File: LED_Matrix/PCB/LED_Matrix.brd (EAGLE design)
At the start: 32 x 32 mm, 8 parts, among them U1 ATTINY48, U2 ULN2803AFWG

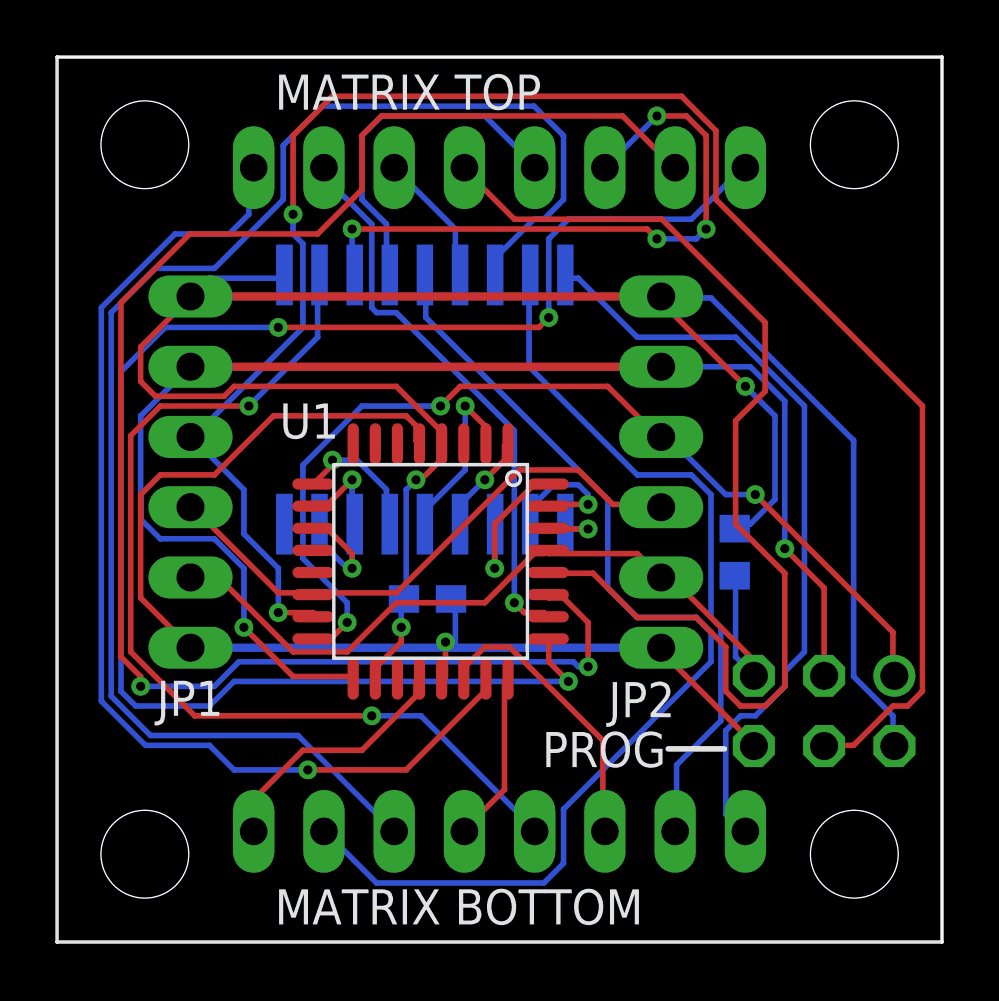
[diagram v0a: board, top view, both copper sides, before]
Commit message: led matrix - Moved library parts local.  Added rev and copyright.
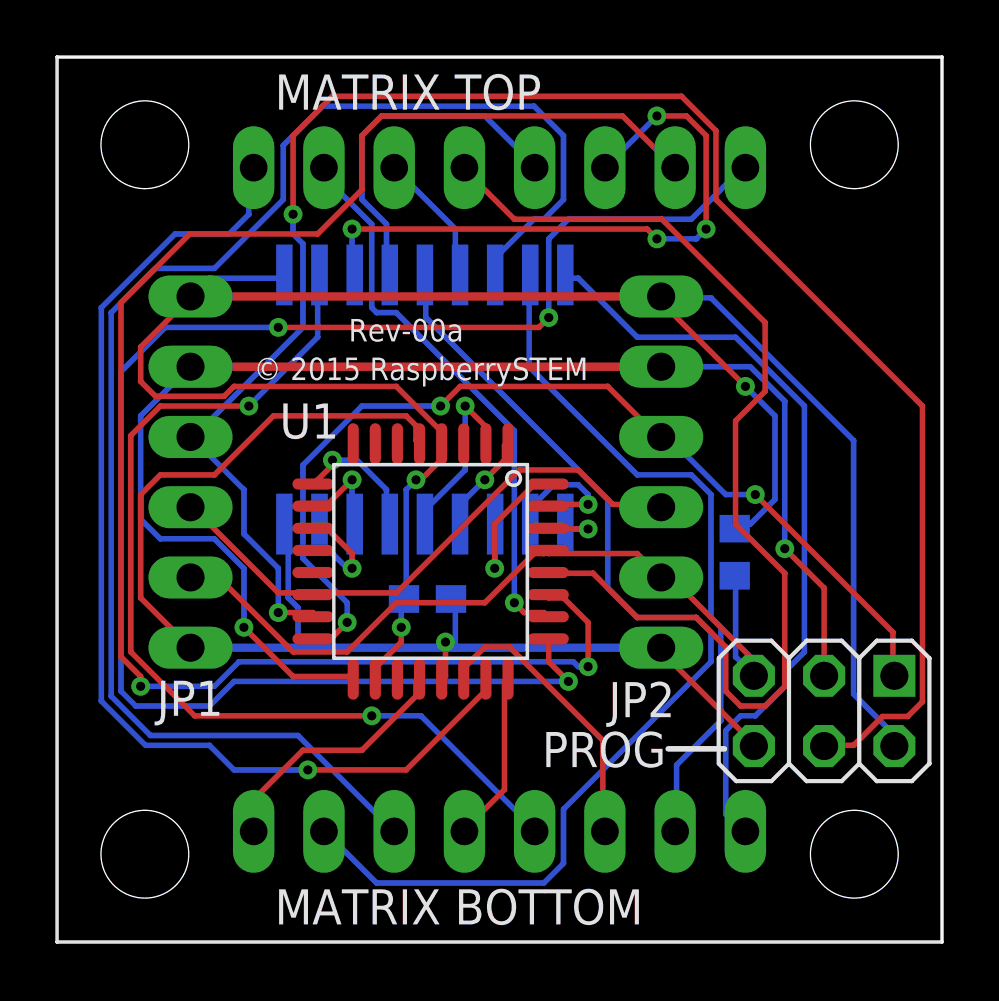
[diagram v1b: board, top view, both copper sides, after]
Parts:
- JP1, JP2: device raspberrystem:1X06 -> LED_Matrix:1X06
- LEDMATRIX: device raspberrystem:8X8_LED_MATRIX -> LED_Matrix:8X8_LED_MATRIX
- PROG: device raspberrystem:MA03-2 -> LED_Matrix:2X03
- U1: device raspberrystem:ATTINY48 -> LED_Matrix:ATTINY48
- U2: device raspberrystem:ULN2803AFWG -> LED_Matrix:ULN2803AFWG
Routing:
- net GND: track 43.7 -> 48.4 mm
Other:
- board text added: "Rev-00a"
- board text added: "© 2015 RaspberrySTEM"
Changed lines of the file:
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@@
 <layer number="56" name="wert" color="7" fill="1" visible="no" active="no"/>
 <layer number="57" name="tCAD" color="7" fill="1" visible="no" active="no"/>
+<layer number="90" name="Modules" color="5" fill="1" visible="no" active="no"/>
 <layer number="91" name="Nets" color="2" fill="1" visible="no" active="no"/>
 <layer number="92" name="Busses" color="1" fill="1" visible="no" active="no"/>
@@
 <wire x1="27.94" y1="13.208" x2="0.381" y2="13.208" width="0.2032" layer="22"/>
 <wire x1="28.829" y1="15.748" x2="0.381" y2="15.748" width="0.2032" layer="22"/>
-<wire x1="26.797" y1="18.288" x2="2.286" y2="18.288" width="0.2032" layer="22"/>
+<wire x1="27.686" y1="18.288" x2="2.286" y2="18.288" width="0.2032" layer="22"/>
 <wire x1="27.686" y1="20.828" x2="0.381" y2="20.828" width="0.2032" layer="22"/>
 <wire x1="27.686" y1="23.368" x2="0.381" y2="23.368" width="0.2032" layer="22"/>
@@
 <text x="2.032" y="17.78" size="1.27" layer="22" font="vector" rot="MR0">IN</text>
 <rectangle x1="0" y1="17.399" x2="2.413" y2="19.431" layer="43"/>
+<text x="7.112" y="20.32" size="0.8128" layer="21">© 2015 RaspberrySTEM</text>
+<text x="10.541" y="21.717" size="0.8128" layer="21">Rev-00a</text>
 </plain>
 <attributes>
@@
 <description language="de">&lt;b&gt;EAGLE Design Rules&lt;/b&gt;
 &lt;p&gt;
-Die Standard-Design-Rules sind so gewÃ¤hlt, dass sie fÃ¼r
+Die Standard-Design-Rules sind so gewÃÂ¤hlt, dass sie fÃÂ¼r
 die meisten Anwendungen passen. Sollte ihre Platine
 besondere Anforderungen haben, treffen Sie die erforderlichen
@@
 </autorouter>
 <elements>
-<element name="U1" library="raspberrystem" package="ATTINY48" value="ATTINY48" x="13.508" y="13.761" smashed="yes" rot="R270">
+<element name="U1" library="LED_Matrix" package="ATTINY48" value="ATTINY48" x="13.508" y="13.761" smashed="yes" rot="R270">
 <attribute name="NAME" x="8.047" y="18.206" size="1.27" layer="21"/>
 </element>
-<element name="U2" library="raspberrystem" package="ULN2803AFWG" value="ULN2803AFWG" x="18.381" y="15.111" smashed="yes" rot="MR0">
+<element name="U2" library="LED_Matrix" package="ULN2803AFWG" value="ULN2803AFWG" x="18.381" y="15.111" smashed="yes" rot="MR0">
 <attribute name="NAME" x="7.205" y="24.636" size="1.27" layer="22" rot="MR0"/>
 </element>
-<element name="LEDMATRIX" library="raspberrystem" package="8X8_LED_MATRIX" value="8X8_LED_MATRIX" x="16" y="16"/>
+<element name="LEDMATRIX" library="LED_Matrix" package="8X8_LED_MATRIX" value="8X8_LED_MATRIX" x="16" y="16"/>
 <element name="R1" library="resistor" package="R0603" value="10k" x="24.5048" y="14.096" smashed="yes" rot="MR270">
 <attribute name="NAME" x="23.3618" y="12.445" size="1.016" layer="26" rot="MR180"/>
@@
 <attribute name="NAME" x="14.5382" y="11.8946" size="1.016" layer="26" rot="MR180"/>
 </element>
-<element name="PROG" library="raspberrystem" package="MA03-2" value="NONE" x="27.7368" y="8.3566" smashed="yes" rot="R180">
-<attribute name="OC_NEWARK" value="unknown" x="27.7368" y="8.3566" size="1.778" layer="27" rot="R180" display="off"/>
-<attribute name="MPN" value="" x="27.7368" y="8.3566" size="1.778" layer="27" rot="R180" display="off"/>
-<attribute name="MF" value="" x="27.7368" y="8.3566" size="1.778" layer="27" rot="R180" display="off"/>
-<attribute name="OC_FARNELL" value="unknown" x="27.7368" y="8.3566" size="1.778" layer="27" rot="R180" display="off"/>
+<element name="PROG" library="LED_Matrix" package="2X03" value="NONE" x="27.7368" y="8.3566" smashed="yes" rot="R180">
 <attribute name="NAME" x="22.0218" y="7.5946" size="1.27" layer="25" ratio="10" rot="R180"/>
 </element>
-<element name="JP1" library="raspberrystem" package="1X06" value="NONE" x="4.826" y="16.9926" smashed="yes" rot="R270">
+<element name="JP1" library="LED_Matrix" package="1X06" value="NONE" x="4.826" y="16.9926" smashed="yes" rot="R270">
 <attribute name="NAME" x="3.6068" y="8.1788" size="1.27" layer="25" ratio="10"/>
 </element>
-<element name="JP2" library="raspberrystem" package="1X06" value="NONE" x="21.844" y="16.9926" smashed="yes" rot="R270">
+<element name="JP2" library="LED_Matrix" package="1X06" value="NONE" x="21.844" y="16.9926" smashed="yes" rot="R270">
 <attribute name="NAME" x="19.939" y="8.128" size="1.27" layer="25" ratio="10"/>
 </element>
@@
 <wire x1="12.6238" y1="12.446" x2="12.5452" y2="12.4026" width="0.2032" layer="16"/>
 <wire x1="13.8684" y1="17.9578" x2="13.908" y2="18.011" width="0.2032" layer="1"/>
-<wire x1="30.226" y1="8.1788" x2="30.226" y2="7.112" width="0.2032" layer="16"/>
-<wire x1="28.8036" y1="9.6012" x2="30.226" y2="8.1788" width="0.2032" layer="16"/>
-<wire x1="28.8036" y1="18.1356" x2="28.8036" y2="9.6012" width="0.2032" layer="16"/>
+<wire x1="30.226" y1="7.5438" x2="30.226" y2="7.112" width="0.2032" layer="16"/>
+<wire x1="28.8036" y1="8.9662" x2="30.226" y2="7.5438" width="0.2032" layer="16"/>
+<wire x1="28.8036" y1="18.1356" x2="28.8036" y2="8.9662" width="0.2032" layer="16"/>
 <wire x1="23.6474" y1="23.2918" x2="28.8036" y2="18.1356" width="0.2032" layer="16"/>
 <wire x1="21.8694" y1="23.2918" x2="23.6474" y2="23.2918" width="0.2032" layer="16"/>
@@
 <contactref element="JP1" pad="6"/>
 <contactref element="JP2" pad="6"/>
-<wire x1="4.826" y1="10.6426" x2="14.0462" y2="10.6426" width="0.3048" layer="16"/>
+<wire x1="4.826" y1="10.6426" x2="8.7122" y2="10.6426" width="0.3048" layer="16"/>
+<wire x1="8.7122" y1="10.6426" x2="14.0462" y2="10.6426" width="0.3048" layer="16"/>
 <wire x1="14.0462" y1="10.6426" x2="14.4018" y2="10.6426" width="0.3048" layer="16"/>
 <wire x1="14.4018" y1="10.6426" x2="21.844" y2="10.6426" width="0.3048" layer="16"/>
@@
 <via x="14.0462" y="10.8458" extent="1-16" drill="0.3302"/>
 <contactref element="U2" pad="GND"/>
-<wire x1="5.6896" y1="16.891" x2="8.221" y2="15.111" width="0" layer="19" extent="1-16"/>
+<wire x1="8.3566" y1="12.446" x2="8.3566" y2="14.9352" width="0.2032" layer="16"/>
+<wire x1="8.7122" y1="12.0904" x2="8.3566" y2="12.446" width="0.2032" layer="16"/>
+<wire x1="8.7122" y1="10.6426" x2="8.7122" y2="12.0904" width="0.2032" layer="16"/>
+<wire x1="8.3566" y1="14.9352" x2="8.221" y2="15.111" width="0.2032" layer="16"/>
 </signal>
 <signal name="SCK">
@@
 <wire x1="4.9784" y1="18.1356" x2="4.826" y2="18.2626" width="0.2032" layer="16"/>
 <wire x1="28.8036" y1="7.112" x2="27.7368" y2="7.112" width="0.2032" layer="1"/>
-<wire x1="30.226" y1="8.5344" x2="28.8036" y2="7.112" width="0.2032" layer="1"/>
-<wire x1="30.7594" y1="8.5344" x2="30.226" y2="8.5344" width="0.2032" layer="1"/>
-<wire x1="31.2928" y1="9.0678" x2="30.7594" y2="8.5344" width="0.2032" layer="1"/>
-<wire x1="31.2928" y1="19.3802" x2="31.2928" y2="9.0678" width="0.2032" layer="1"/>
+<wire x1="29.845" y1="8.1534" x2="28.8036" y2="7.112" width="0.2032" layer="1"/>
+<wire x1="30.7594" y1="8.1534" x2="29.845" y2="8.1534" width="0.2032" layer="1"/>
+<wire x1="31.2928" y1="8.6868" x2="30.7594" y2="8.1534" width="0.2032" layer="1"/>
+<wire x1="31.2928" y1="19.3802" x2="31.2928" y2="8.6868" width="0.2032" layer="1"/>
 <wire x1="23.8252" y1="26.8478" x2="31.2928" y2="19.3802" width="0.2032" layer="1"/>
 <wire x1="23.8252" y1="29.337" x2="23.8252" y2="26.8478" width="0.2032" layer="1"/>
@@
 </signal>
 </signals>
-<errors>
-</errors>
 </board>
 </drawing>

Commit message: led matrix - fixed silkscreen and flipped prog header
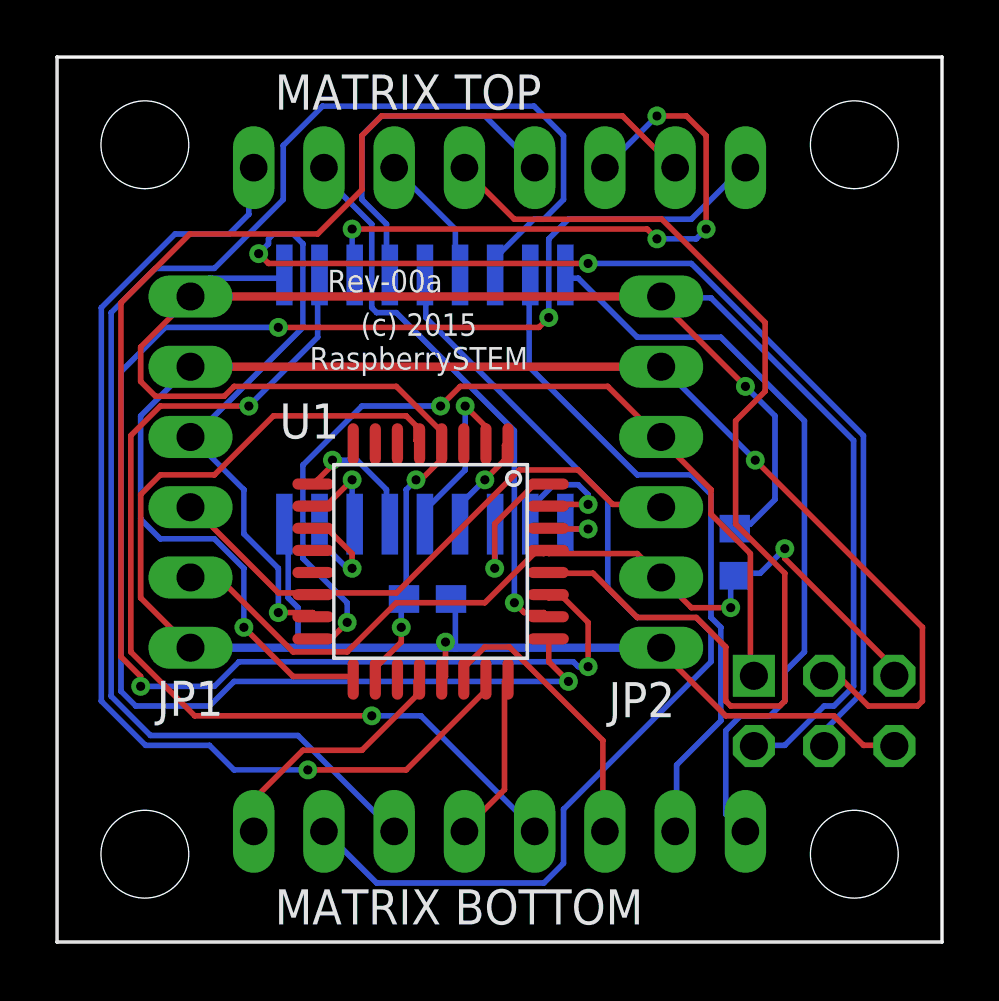
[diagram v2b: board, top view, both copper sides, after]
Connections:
- net GND: now also PROG.2; no longer PROG.6
- net MISO: now also PROG.5; no longer PROG.1
- net RESET: now also PROG.1; no longer PROG.5
- net VCC: now also PROG.6; no longer PROG.2
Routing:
- net MOSI: track 66.2 -> 56.3 mm, vias 2 -> 3
- net GND: track 48.4 -> 53.4 mm
- net SCK: track 50.1 -> 54.8 mm
- net RESET: track 29.1 -> 32.9 mm, vias 0 -> 2
- net MISO: track 35.6 -> 32.7 mm, vias 3 -> 2
- net VCC: track 78.5 -> 80.2 mm
- net ROW7: track 39.3 -> 39.9 mm
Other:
- board text added: "(c) 2015 RaspberrySTEM"
- board text added: "3.3V"
- board text added: "CE"
- board text added: "MISO"
- board text added: "SCLK"
- board text added: "SI"
- board text removed: "CLK"
- board text removed: "CS"
- board text removed: "IN"
- board text removed: "OUT"
- board text removed: "VCC"
- board text removed: "© 2015 RaspberrySTEM"
